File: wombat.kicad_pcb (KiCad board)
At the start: 2 copper layers, 246.8 x 76.2 mm, 198 parts, among them J1 Conn_01x01, J2 Conn_01x01, SW1 SW_SPST, SW10 SW_SPST, SW101 SW_Push, SW11 SW_SPST, SW12 SW_SPST, SW13 SW_SPST, SW14 SW_SPST, SW15 SW_SPST, SW16 SW_SPST, SW17 SW_SPST, SW18 SW_SPST, SW19 SW_SPST, SW2 SW_SPST, SW20 SW_SPST, SW21 SW_SPST, SW22 SW_SPST, SW23 SW_SPST, SW24 SW_SPST, SW25 SW_SPST, SW26 SW_SPST, SW27 SW_SPST, SW28 SW_SPST, SW29 SW_SPST, SW3 SW_SPST, SW30 SW_SPST, SW31 SW_SPST, SW32 SW_SPST, SW33 SW_SPST, SW34 SW_SPST, SW35 SW_SPST, SW36 SW_SPST, SW37 SW_SPST, SW38 SW_SPST, SW39 SW_SPST, SW4 SW_SPST, SW40 SW_SPST, SW41 SW_SPST, SW42 SW_SPST, SW43 SW_SPST, SW44 SW_SPST, SW45 SW_SPST, SW46 SW_SPST, SW5 SW_SPST, SW6 SW_SPST, SW7 SW_SPST, SW8 SW_SPST, SW9 SW_SPST, U1 ProMicro

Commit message: change orientation of mc
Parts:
- added G***: LOGO, lib:wombat_animal, B.Cu at (251.0, 71.2)
- G***: moved to F.Cu
- G***, U1: moved to B.Cu
- SW101: footprint Button_Switch_SMD:SW_Push_1P1T_NO_6x6mm_H9.5mm -> Button_Switch_SMD:SW_SPST_EVQP0
- moved G*** 111.3 mm to (49.9, 96.9), turned to 0 degrees
- moved D39 17.9 mm to (246.3, 88.3)
- moved D43 13.6 mm to (267.4, 88.1), turned to 90 degrees
- moved R113 10.6 mm to (247.7, 82.2)
- moved D40 5.43 mm to (246.3, 95.4)
- moved D44 5.38 mm to (267.4, 95.4)
- moved G*** 2.79 mm to (145.7, 101.5), turned to 173 degrees
- moved J1 1.25 mm to (241.6, 114.8)
- moved J2 1.25 mm to (241.6, 107.7)
- moved U1 1.00 mm to (256.8, 71.1)
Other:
- board size 246.8 x 76.2 mm -> 247.4 x 76.2 mm
- board text added: "github.com/egladman/wombat-pcb"

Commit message: route traces
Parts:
- removed G***: LOGO, lib:wombat_animal
- removed G***: LOGO, lib:oshw_logo
- removed REF** (x5): MountingHole_2.2mm_M2_DIN965_Pad, MountingHole:MountingHole_2.2mm_M2_DIN965_Pad
- added G1: LOGO, lib:oshw_logo, F.Cu at (47.2, 94.1)
- added H3: MountingHole_2.2mm_M2_DIN965_Pad, MountingHole:MountingHole_2.2mm_M2_DIN965_Pad, F.Cu at (198.0, 133.0)
- added H4: MountingHole_2.2mm_M2_DIN965_Pad, MountingHole:MountingHole_2.2mm_M2_DIN965_Pad, F.Cu at (265.0, 102.0)
- added H5: MountingHole_2.2mm_M2_DIN965_Pad, MountingHole:MountingHole_2.2mm_M2_DIN965_Pad, F.Cu at (151.6, 99.0)
- added H6: MountingHole_2.2mm_M2_DIN965_Pad, MountingHole:MountingHole_2.2mm_M2_DIN965_Pad, F.Cu at (42.6, 69.0)
- added H8: MountingHole_2.2mm_M2_DIN965_Pad, MountingHole:MountingHole_2.2mm_M2_DIN965_Pad, F.Cu at (232.0, 68.0)
- R113: footprint Resistor_SMD:R_0805_2012Metric_Pad1.15x1.40mm_HandSolder -> lib:R_0805_2012Metric_Pad1.15x1.40mm_HandSolder_Double_Sided
- moved R113 15.8 mm to (251.1, 66.8), turned to 90 degrees
- moved U1 1.40 mm to (258.2, 71.1)
- renumbered G*** to G3, REF** to H1, REF** to H2, REF** to H7
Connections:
- SW101 pad 2: /bk_GND -> Net-(SW101-Pad2)
- U1 pad 23: /bk_GND -> Net-(SW101-Pad2)
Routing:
- net /bk_PWM: track 0.00 -> 1003.4 mm, vias 0 -> 1
- net /bk_GND: track 0.00 -> 931.7 mm
- net /col_4: track 0.00 -> 307.9 mm, vias 0 -> 2
- net /row_3: track 0.00 -> 305.7 mm, vias 0 -> 1
- net /row_0: track 0.00 -> 278.5 mm
- net /row_2: track 0.00 -> 257.9 mm
- net /col_5: track 0.00 -> 254.5 mm
- net /col_1: track 0.00 -> 251.7 mm, vias 0 -> 1
- net /row_1: track 0.00 -> 242.9 mm
- net /col_3: track 0.00 -> 240.4 mm, vias 0 -> 1
- net /col_2: track 0.00 -> 234.7 mm
- net /col_0: track 0.00 -> 225.9 mm
- net /col_6: track 0.00 -> 217.6 mm
- net /col_7: track 0.00 -> 200.0 mm, vias 0 -> 1
- net /col_8: track 0.00 -> 191.2 mm
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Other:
- board size 247.4 x 76.2 mm -> 250.5 x 77.4 mm
- net class Power added: clearance 0.5, trace_width 0.55, via_dia 1.1, via_drill 0.7
- board text added: "haphazardly designed by Eli Gladman"
- board text removed: "Designed By Eli Gladman"

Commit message: Add ground zones
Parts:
- added G2: LOGO, lib:wombat_animal, B.Cu at (325.2, 38.9)
- moved G1 82.4 mm to (123.0, 126.5)
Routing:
- added copper zone on B.Cu, net (none)
- added copper zone on F.Cu, net (none)
- added copper zone on B.Cu, net /bk_GND
- added copper zone on F.Cu, net /bk_GND

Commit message: adjust ground zones
tweak ground zones near pro micro headers
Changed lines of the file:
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@@
   (page A4)
   (layers
-    (0 F.Cu signal hide)
-    (31 B.Cu signal)
+    (0 F.Cu signal)
+    (31 B.Cu signal hide)
     (32 B.Adhes user hide)
     (33 F.Adhes user hide)
@@
     (polygon
       (pts
-        (xy 272.38348 61.582352) (xy 272.38348 65.727318) (xy 267.646376 65.727318) (xy 267.646376 76.385802) (xy 272.38348 76.385802)
-        (xy 272.38348 80.530768) (xy 270.014928 80.530768) (xy 270.014928 134.415326) (xy 267.054238 137.376016) (xy 26.64621 137.376016)
+        (xy 272.975618 61.582352) (xy 272.975618 65.727318) (xy 267.646376 65.727318) (xy 267.646376 76.385802) (xy 272.975618 76.385802)
+        (xy 272.975618 80.530768) (xy 270.014928 80.530768) (xy 270.014928 134.415326) (xy 267.054238 137.376016) (xy 26.64621 137.376016)
         (xy 23.68552 134.415326) (xy 23.68552 64.543042) (xy 26.64621 61.582352)
       )
     )
   )
-  (zone (net 52) (net_name /bk_GND) (layer B.Cu) (hatch edge 0.508)
-    (connect_pads (clearance 0.508))
-    (min_thickness 0.254)
-    (fill yes (arc_segments 32) (thermal_gap 0.508) (thermal_bridge_width 0.508))
-    (polygon
-      (pts
-        (xy 26.64621 61.582352) (xy 23.68552 64.543042) (xy 23.68552 134.415326) (xy 26.64621 137.376016) (xy 267.054238 137.376016)
-        (xy 270.014928 134.415326) (xy 270.014928 80.530768) (xy 272.38348 80.530768) (xy 272.38348 76.385802) (xy 267.646376 76.385802)
-        (xy 267.646376 65.727318) (xy 272.38348 65.727318) (xy 272.38348 61.582352)
-      )
-    )
-  )
   (zone (net 52) (net_name /bk_GND) (layer F.Cu) (hatch edge 0.508)
     (connect_pads (clearance 0.508))
@@
       (pts
         (xy 26.64621 61.582352) (xy 23.68552 64.543042) (xy 23.68552 134.415326) (xy 26.64621 137.376016) (xy 267.054238 137.376016)
-        (xy 270.014928 134.415326) (xy 270.014928 80.530768) (xy 272.38348 80.530768) (xy 272.38348 76.385802) (xy 267.646376 76.385802)
+        (xy 270.014928 134.415326) (xy 270.014928 80.530768) (xy 272.975618 80.530768) (xy 272.975618 76.385802) (xy 267.646376 76.385802)
         (xy 267.646376 65.727318) (xy 272.38348 65.727318) (xy 272.38348 61.582352)
       )
@@
       (pts
         (xy 26.64621 61.582352) (xy 23.68552 64.543042) (xy 23.68552 134.415326) (xy 26.64621 137.376016) (xy 267.054238 137.376016)
-        (xy 270.014928 134.415326) (xy 270.014928 80.530768) (xy 272.38348 80.530768) (xy 272.38348 76.385802) (xy 267.646376 76.385802)
-        (xy 267.646376 65.727318) (xy 272.38348 65.727318) (xy 272.38348 61.582352)
+        (xy 270.014928 134.415326) (xy 270.014928 80.530768) (xy 272.975618 80.530768) (xy 272.975618 76.385802) (xy 267.646376 76.385802)
+        (xy 267.646376 65.727318) (xy 272.975618 65.727318) (xy 272.975618 61.582352)
       )
     )
@@
       (pts
         (xy 26.64621 61.582352) (xy 23.68552 64.543042) (xy 23.68552 134.415326) (xy 26.64621 137.376016) (xy 267.054238 137.376016)
-        (xy 270.014928 134.415326) (xy 270.014928 80.530768) (xy 272.38348 80.530768) (xy 272.38348 76.385802) (xy 267.646376 76.385802)
-        (xy 267.646376 65.727318) (xy 272.38348 65.727318) (xy 272.38348 61.582352)
+        (xy 270.014928 134.415326) (xy 270.014928 80.530768) (xy 272.975618 80.530768) (xy 272.975618 76.385802) (xy 267.646376 76.385802)
+        (xy 267.646376 65.727318) (xy 272.975618 65.727318) (xy 272.975618 61.582352)
       )
     )

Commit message: removed old asset
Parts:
- removed G2: LOGO, lib:wombat_animal
- moved D46 1.07 mm to (267.1, 128.8)
- moved SW46 1.07 mm to (257.6, 128.8)
- moved D43 1.07 mm to (266.8, 89.0)
- moved R125 1.07 mm to (257.6, 100.4)
- moved R146 1.07 mm to (263.7, 133.5)
- moved SW43 1.07 mm to (259.9, 71.9)
- moved SW44 1.07 mm to (257.6, 90.9)
- moved D103 1.07 mm to (69.2, 77.0)
- moved D105 1.07 mm to (107.1, 77.4)
- moved D106 1.07 mm to (126.0, 77.4)
- moved D107 1.07 mm to (144.9, 77.4)
- moved D108 1.07 mm to (163.9, 77.4)
- moved D109 1.07 mm to (182.9, 77.4)
- moved D110 1.07 mm to (201.8, 77.4)
- moved D111 1.07 mm to (220.8, 77.4)
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
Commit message: Update wombat.kicad_pcb
add addidtional silkscreen annotation for R113
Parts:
- added ?: , , F.Cu at (289.3, -27.5)
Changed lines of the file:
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@@
     (tracks 1537)
     (zones 0)
-    (modules 198)
+    (modules 199)
     (nets 116)
   )
   (page A4)
   (layers
-    (0 F.Cu signal)
-    (31 B.Cu signal)
+    (0 F.Cu signal hide)
+    (31 B.Cu signal hide)
     (32 B.Adhes user)
-    (33 F.Adhes user)
+    (33 F.Adhes user hide)
     (34 B.Paste user)
     (35 F.Paste user)
@@
     (add_net "Net-(D146-Pad2)")
   )
+  (module "" (layer F.Cu)
+    (at 289.259413 -27.534417)
+    (fp_text reference "" (at 122.407862 127.388207) (layer F.SilkS)
+      (effects (font (size 1.27 1.27) (thickness 0.15)))
+    )
+    (fp_text value "" (at 122.407862 127.388207) (layer F.SilkS)
+      (effects (font (size 1.27 1.27) (thickness 0.15)))
+    )
+    (fp_text user R113 (at -37.037413 95.225417 90) (layer B.SilkS)
+      (effects (font (size 1 1) (thickness 0.15)) (justify mirror))
+    )
+  )
   (module lib:oshw_logo (layer F.Cu)

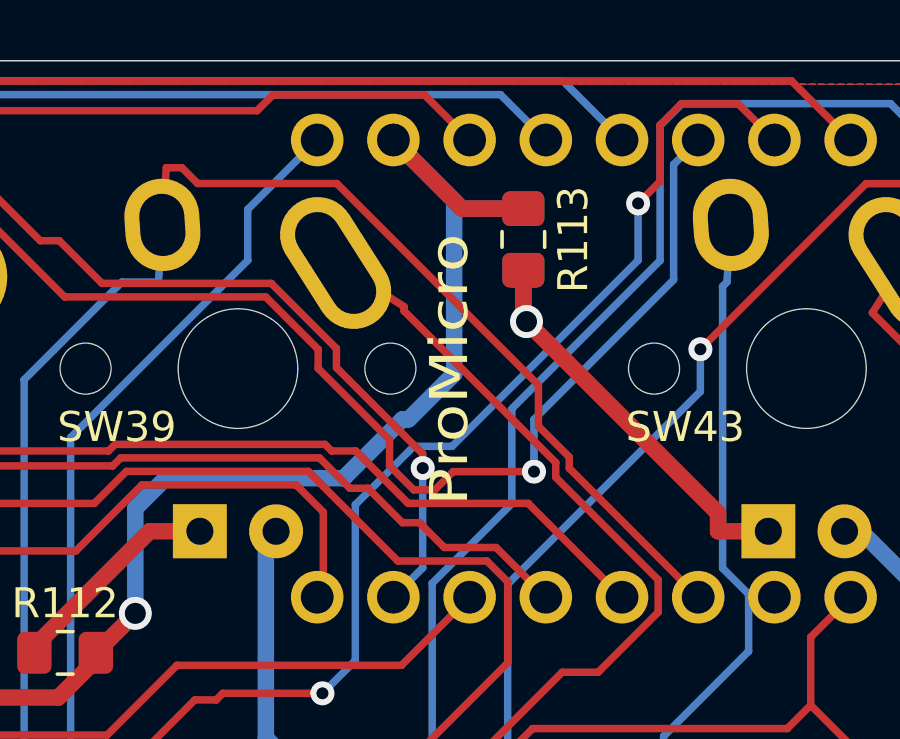
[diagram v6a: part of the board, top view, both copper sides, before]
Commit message: hide fab values
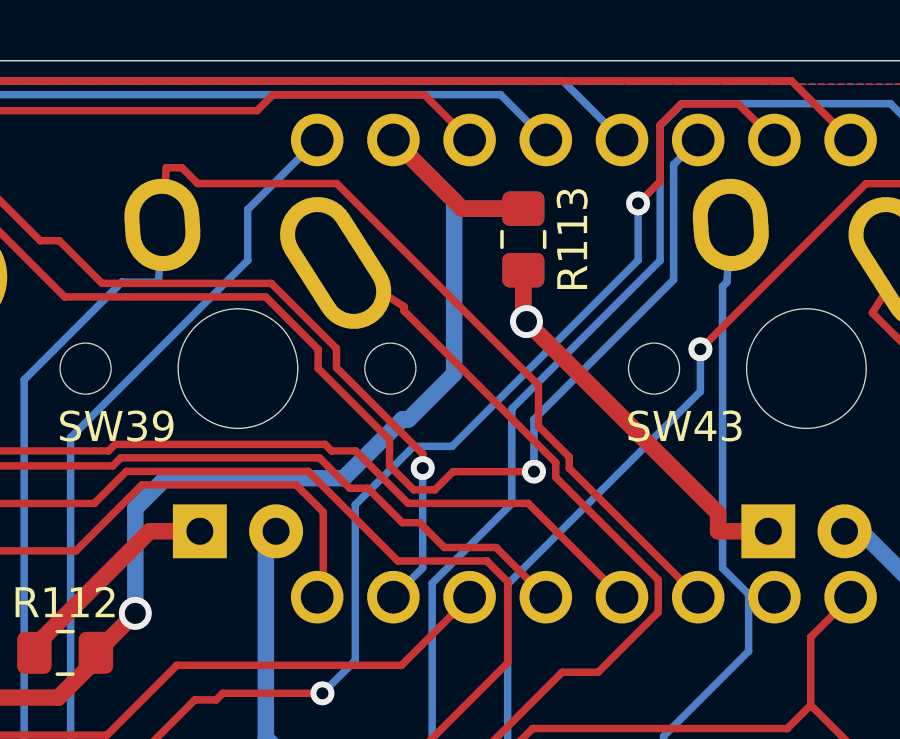
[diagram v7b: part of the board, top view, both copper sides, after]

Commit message: Support bottom row variant
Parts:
- removed ?: , 
- removed D136, D137, D138, D139, D140, D141, D142, D143, D144, D145, D146: LED, keebs-github:LED_D2.0mm_W4.8mm_H2.5mm_FlatTop_Reverse_Polarity
- removed R136, R137, R138, R139, R140, R141, R142, R143, R144, R145, R146: 300, Resistor_SMD:R_0805_2012Metric_Pad1.15x1.40mm_HandSolder
- added SW47: SW_SPST, keebs-github:Mx_Alps_200, B.Cu at (179.4, 128.8)
- added SW48: SW_SPST, keebs-github:Mx_Alps_225, B.Cu at (139.2, 128.8)
- added SW49: SW_SPST, keebs-github:Mx_Alps_125, B.Cu at (106.0, 128.8)
- added SW50: SW_SPST, keebs-github:Mx_Alps_125, B.Cu at (82.3, 128.8)
- added SW51: SW_SPST, keebs-github:Mx_Alps_125, B.Cu at (58.6, 128.8)
- added SW52: SW_SPST, keebs-github:Mx_Alps_125, B.Cu at (34.9, 128.8)
- D10, D11, D12, D13, D14, D15, D16, D17, D18, D19, D2, D20, D21, D22, D23, D24, D25, D26, D27, D28, D29, D3, D30, D31, D32, D33, D34, D35, D36, D37, D38, D39, D4, D40, D41, D42, D43, D44, D45, D46, D5, D6, D7, D8, D9: footprint Diode_SMD:D_SOD-123 -> Diode_SMD:D_0805_2012Metric_Pad1.15x1.40mm_HandSolder
- H2, H5: value MountingHole_2.2mm_M2_DIN965_Pad -> MountingHole_2.2mm_M2_DIN965_Pad_Oval; footprint MountingHole:MountingHole_2.2mm_M2_DIN965_Pad -> lib:MountingHole_2.2mm_M2_DIN965_Pad_Oval
- J1: value Conn_01x01 -> Conn_01x02; footprint Connector_Wire:SolderWirePad_1x01_Drill0.8mm -> Connector_Wire:SolderWirePad_1x02_P3.81mm_Drill1.2mm
- J2: value Conn_01x01 -> Conn_01x03; footprint Connector_Wire:SolderWirePad_1x01_Drill0.8mm -> Connector_Wire:SolderWirePad_1x03_P3.81mm_Drill1.2mm
- R113: footprint lib:R_0805_2012Metric_Pad1.15x1.40mm_HandSolder_Double_Sided -> Resistor_SMD:R_0805_2012Metric_Pad1.15x1.40mm_HandSolder
- moved D113 195.1 mm to (64.5, 96.0)
- moved R113 187.7 mm to (65.7, 100.4), turned to 0 degrees
- moved R125 164.5 mm to (94.1, 119.3)
- moved D125 164.5 mm to (92.9, 114.9)
- moved R123 162.2 mm to (56.3, 119.3)
- moved D123 162.2 mm to (55.0, 114.9)
- moved R124 162.2 mm to (75.2, 119.3)
- moved D124 162.2 mm to (73.9, 114.9)
- moved R133 94.3 mm to (263.2, 132.9), turned to 90 degrees
- moved D133 90.3 mm to (257.0, 133.5)
- moved R128 83.0 mm to (158.2, 119.0)
- moved R129 81.0 mm to (175.1, 119.3)
- moved D126 78.2 mm to (111.8, 114.9)
- moved R126 78.2 mm to (113.1, 119.3)
- moved D129 75.8 mm to (168.7, 114.9)
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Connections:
- D101 pad 1: /bk_GND -> GND
- D102 pad 1: /bk_GND -> GND
- D103 pad 1: /bk_GND -> GND
- D104 pad 1: /bk_GND -> GND
- D105 pad 1: /bk_GND -> GND
- D106 pad 1: /bk_GND -> GND
- D107 pad 1: /bk_GND -> GND
- D108 pad 1: /bk_GND -> GND
- D109 pad 1: /bk_GND -> GND
- D110 pad 1: /bk_GND -> GND
- D111 pad 1: /bk_GND -> GND
- D112 pad 1: /bk_GND -> GND
- D113 pad 1: /bk_GND -> GND
- D114 pad 1: /bk_GND -> GND
- D115 pad 1: /bk_GND -> GND
- D116 pad 1: /bk_GND -> GND
- D117 pad 1: /bk_GND -> GND
- D118 pad 1: /bk_GND -> GND
- D119 pad 1: /bk_GND -> GND
- D120 pad 1: /bk_GND -> GND
- D121 pad 1: /bk_GND -> GND
- D122 pad 1: /bk_GND -> GND
- D123 pad 1: /bk_GND -> GND
- D124 pad 1: /bk_GND -> GND
- D125 pad 1: /bk_GND -> GND
- D126 pad 1: /bk_GND -> GND
- D127 pad 1: /bk_GND -> GND
- D128 pad 1: /bk_GND -> GND
- D129 pad 1: /bk_GND -> GND
- D130 pad 1: /bk_GND -> GND
- D131 pad 1: /bk_GND -> GND
- D132 pad 1: /bk_GND -> GND
- D133 pad 1: /bk_GND -> GND
- D134 pad 1: /bk_GND -> GND
- D135 pad 1: /bk_GND -> GND
- J1 pad 1: /bk_GND -> +5V
- J2 pad 1: Net-(J2-Pad1) -> /AUX_LED_VCC_C
- R101 pad 2: /bk_PWM -> /BACKLIGHT_PWM
- R102 pad 2: /bk_PWM -> /BACKLIGHT_PWM
- R103 pad 2: /bk_PWM -> /BACKLIGHT_PWM
- R104 pad 2: /bk_PWM -> /BACKLIGHT_PWM
- R105 pad 2: /bk_PWM -> /BACKLIGHT_PWM
- R106 pad 2: /bk_PWM -> /BACKLIGHT_PWM
- R107 pad 2: /bk_PWM -> /BACKLIGHT_PWM
- R108 pad 2: /bk_PWM -> /BACKLIGHT_PWM
- R109 pad 2: /bk_PWM -> /BACKLIGHT_PWM
- R110 pad 2: /bk_PWM -> /BACKLIGHT_PWM
- R111 pad 2: /bk_PWM -> /BACKLIGHT_PWM
- R112 pad 2: /bk_PWM -> /BACKLIGHT_PWM
- R113 pad 2: /bk_PWM -> /BACKLIGHT_PWM
- R114 pad 2: /bk_PWM -> /BACKLIGHT_PWM
- R115 pad 2: /bk_PWM -> /BACKLIGHT_PWM
- R116 pad 2: /bk_PWM -> /BACKLIGHT_PWM
- R117 pad 2: /bk_PWM -> /BACKLIGHT_PWM
- R118 pad 2: /bk_PWM -> /BACKLIGHT_PWM
- R119 pad 2: /bk_PWM -> /BACKLIGHT_PWM
- R120 pad 2: /bk_PWM -> /BACKLIGHT_PWM
- R121 pad 2: /bk_PWM -> /BACKLIGHT_PWM
- R122 pad 2: /bk_PWM -> /BACKLIGHT_PWM
- R123 pad 2: /bk_PWM -> /BACKLIGHT_PWM
- R124 pad 2: /bk_PWM -> /BACKLIGHT_PWM
- R125 pad 2: /bk_PWM -> /BACKLIGHT_PWM
- R126 pad 2: /bk_PWM -> /BACKLIGHT_PWM
- R127 pad 2: /bk_PWM -> /BACKLIGHT_PWM
- R128 pad 2: /bk_PWM -> /BACKLIGHT_PWM
- R129 pad 2: /bk_PWM -> /BACKLIGHT_PWM
- R130 pad 2: /bk_PWM -> /BACKLIGHT_PWM
- R131 pad 2: /bk_PWM -> /BACKLIGHT_PWM
- R132 pad 2: /bk_PWM -> /BACKLIGHT_PWM
- R133 pad 2: /bk_PWM -> /AUX_LED_VCC_A
- R134 pad 2: /bk_PWM -> /AUX_LED_VCC_B
- R135 pad 2: /bk_PWM -> /AUX_LED_VCC_C
- SW1 pad 2: /col_0 -> Net-(SW1-Pad2)
- U1 pad 14: /bk_PWM -> /BACKLIGHT_PWM
- U1 pad 21: Net-(J2-Pad1) -> +5V
- U1 pad 3: /bk_GND -> GND
- U1 pad 4: /bk_GND -> GND
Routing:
- net /bk_PWM: track 1003.4 -> 0.00 mm, vias 1 -> 0
- net /bk_GND: track 931.7 -> 0.00 mm
- net /col_4: track 307.9 -> 0.00 mm, vias 2 -> 0
- net /row_3: track 305.7 -> 0.00 mm, vias 1 -> 0
- net /row_0: track 278.5 -> 0.00 mm
- net /row_2: track 257.9 -> 0.00 mm
- net /col_5: track 254.5 -> 0.93 mm
- net /col_1: track 251.7 -> 0.00 mm, vias 1 -> 0
- net /row_1: track 242.9 -> 0.00 mm
- net /col_3: track 240.4 -> 0.00 mm, vias 1 -> 0
- net /col_2: track 234.7 -> 0.00 mm
- net /col_0: track 225.9 -> 0.00 mm
- net /col_6: track 217.6 -> 0.00 mm
- net /col_7: track 200.0 -> 0.00 mm, vias 1 -> 0
- net /col_8: track 191.2 -> 0.39 mm
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- added copper zone on B.Cu, net GND
- added copper zone on F.Cu, net GND
- removed copper zone on B.Cu, net /bk_GND
- removed copper zone on F.Cu, net /bk_GND
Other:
- board text added: "GND"
- board text added: "LED A"
- board text added: "LED B"
- board text added: "LED C"
- board text added: "Rev C"
- board text added: "VCC"
- board text removed: "Rev B"
- board text removed: "gnd"
- board text removed: "vcc"
